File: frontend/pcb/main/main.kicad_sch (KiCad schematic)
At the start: 57 parts, among them J1 Ext, J10 Display1443, J2 CONN_01X02, J3 Display4020, J4 Debug, J5 RS485, J6 Conn_01x04, J7 Conn_01x02, J8 Conn_01x02, J9 Conn_01x02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

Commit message: Place remaining components.
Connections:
- net +12V: now also K1.4; no longer K1.3
- net GND: now also J2.2 (Pin_2); no longer J2.1 (Pin_1)
- new net: J2.1 (Pin_1), K1.3
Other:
- moved on the sheet: J2
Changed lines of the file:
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@@
     (stroke (width 0) (type solid))
+  )
+  (wire (pts (xy 231.14 143.51) (xy 231.14 138.43))
+    (stroke (width 0) (type default))
   )
   (wire (pts (xy 241.3 139.7) (xy 241.3 140.97))
@@
     (stroke (width 0) (type default))
   )
+  (wire (pts (xy 228.6 123.19) (xy 228.6 121.285))
+    (stroke (width 0) (type default))
+  )
   (wire (pts (xy 278.13 118.11) (xy 278.13 120.65))
     (stroke (width 0) (type default))
@@
     (stroke (width 0) (type default))
   )
+  (wire (pts (xy 219.71 149.86) (xy 217.17 149.86))
+    (stroke (width 0) (type default))
+  )
   (wire (pts (xy 124.46 44.45) (xy 147.955 44.45))
     (stroke (width 0) (type default))
@@
     (stroke (width 0) (type default))
   )
+  (wire (pts (xy 228.6 121.285) (xy 219.71 121.285))
+    (stroke (width 0) (type default))
+  )
   (wire (pts (xy 232.41 204.47) (xy 232.41 207.01))
     (stroke (width 0) (type default))
@@
   (wire (pts (xy 232.41 210.82) (xy 261.62 210.82))
     (stroke (width 0) (type default))
-  )
-  (wire (pts (xy 231.14 138.43) (xy 231.14 149.86))
-    (stroke (width 0) (type solid))
   )
   (wire (pts (xy 265.43 71.12) (xy 265.43 72.39))
@@
     (stroke (width 0) (type default))
   )
+  (wire (pts (xy 219.71 121.285) (xy 219.71 149.86))
+    (stroke (width 0) (type default))
+  )
   (wire (pts (xy 46.99 147.32) (xy 63.5 147.32))
     (stroke (width 0) (type default))
   )
-  (wire (pts (xy 228.6 113.03) (xy 228.6 123.19))
-    (stroke (width 0) (type solid))
-  )
   (wire (pts (xy 245.11 53.34) (xy 245.11 55.88))
     (stroke (width 0) (type default))
@@
   )
   (wire (pts (xy 200.66 216.535) (xy 200.66 217.805))
-    (stroke (width 0) (type default))
-  )
-  (wire (pts (xy 231.14 149.86) (xy 217.17 149.86))
     (stroke (width 0) (type default))
   )
@@
     (stroke (width 0) (type default))
   )
+  (wire (pts (xy 226.06 143.51) (xy 231.14 143.51))
+    (stroke (width 0) (type default))
+  )
   (wire (pts (xy 142.24 130.175) (xy 146.05 130.175))
     (stroke (width 0) (type default))
@@
   )
   (wire (pts (xy 132.08 147.955) (xy 132.08 159.385))
+    (stroke (width 0) (type default))
+  )
+  (wire (pts (xy 226.06 140.97) (xy 226.06 143.51))
     (stroke (width 0) (type default))
   )
@@
     )
   )
-  (symbol (lib_id "power:+12V") (at 228.6 113.03 0) (unit 1)
-    (exclude_from_sim no) (in_bom yes) (on_board yes) (dnp no) (fields_autoplaced)
-    (property "Reference" "#PWR04" (at 228.6 116.84 0)
-      (effects (font (size 1.27 1.27)) hide)
-    )
-    (property "Value" "+12V" (at 228.6 109.22 0)
+  (symbol (lib_id "power:+12V") (at 226.06 140.97 0) (unit 1)
+    (exclude_from_sim no) (in_bom yes) (on_board yes) (dnp no) (fields_autoplaced)
+    (property "Reference" "#PWR04" (at 226.06 144.78 0)
+      (effects (font (size 1.27 1.27)) hide)
+    )
+    (property "Value" "+12V" (at 226.06 137.16 0)
       (effects (font (size 1.27 1.27)))
     )
-    (property "Footprint" "" (at 228.6 113.03 0)
-      (effects (font (size 1.27 1.27)) hide)
-    )
-    (property "Datasheet" "" (at 228.6 113.03 0)
-      (effects (font (size 1.27 1.27)) hide)
-    )
-    (property "Description" "" (at 228.6 113.03 0)
+    (property "Footprint" "" (at 226.06 140.97 0)
+      (effects (font (size 1.27 1.27)) hide)
+    )
+    (property "Datasheet" "" (at 226.06 140.97 0)
+      (effects (font (size 1.27 1.27)) hide)
+    )
+    (property "Description" "" (at 226.06 140.97 0)
       (effects (font (size 1.27 1.27)) hide)
     )
@@
     )
   )
-  (symbol (lib_id "Connector_Generic:Conn_01x02") (at 212.09 152.4 180) (unit 1)
+  (symbol (lib_id "Connector_Generic:Conn_01x02") (at 212.09 149.86 0) (mirror y) (unit 1)
     (exclude_from_sim no) (in_bom yes) (on_board yes) (dnp no)
-    (property "Reference" "J2" (at 212.09 156.21 0)
+    (property "Reference" "J2" (at 212.09 146.05 0)
       (effects (font (size 1.27 1.27)))
     )
-    (property "Value" "CONN_01X02" (at 209.55 152.4 90)
-      (effects (font (size 1.27 1.27)) hide)
-    )
-    (property "Footprint" "Connector_JST:JST_XH_B2B-XH-A_1x02_P2.50mm_Vertical" (at 212.09 152.4 0)
-      (effects (font (size 1.27 1.27)) hide)
-    )
-    (property "Datasheet" "~" (at 212.09 152.4 0)
-      (effects (font (size 1.27 1.27)) hide)
-    )
-    (property "Description" "" (at 212.09 152.4 0)
-      (effects (font (size 1.27 1.27)) hide)
-    )
+    (property "Value" "CONN_01X02" (at 209.55 149.86 90)
+      (effects (font (size 1.27 1.27)) hide)
+    )
+    (property "Footprint" "Connector_JST:JST_XH_B2B-XH-A_1x02_P2.50mm_Vertical" (at 212.09 149.86 0)
+      (effects (font (size 1.27 1.27)) hide)
+    )
+    (property "Datasheet" "~" (at 212.09 149.86 0)
+      (effects (font (size 1.27 1.27)) hide)
+    )
+    (property "Description" "" (at 212.09 149.86 0)
+      (effects (font (size 1.27 1.27)) hide)
+    )

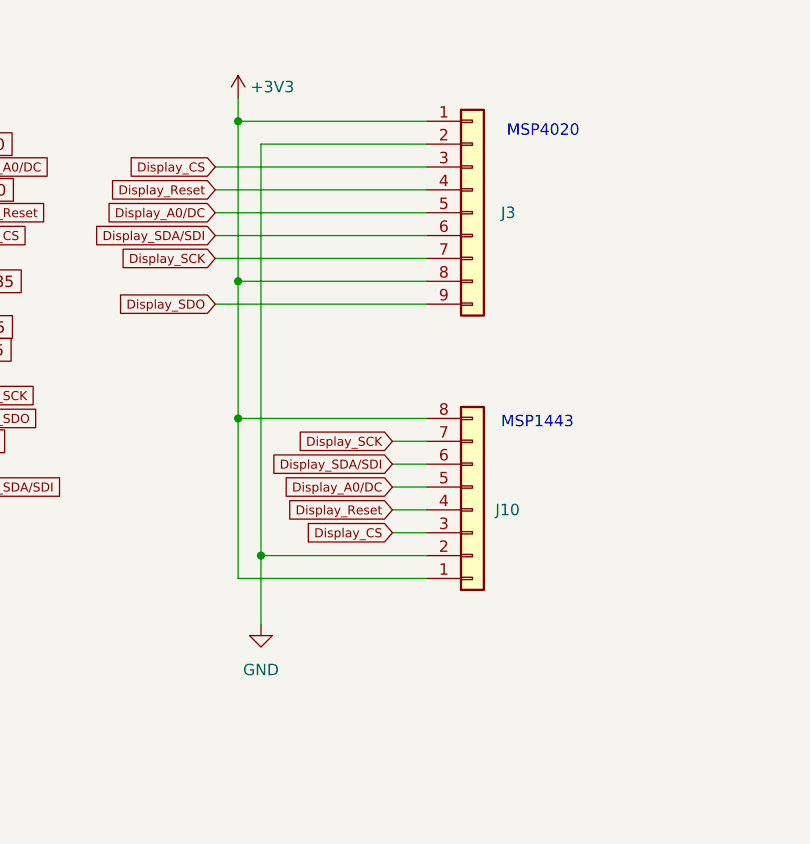
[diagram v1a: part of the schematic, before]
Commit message: Complete routing.
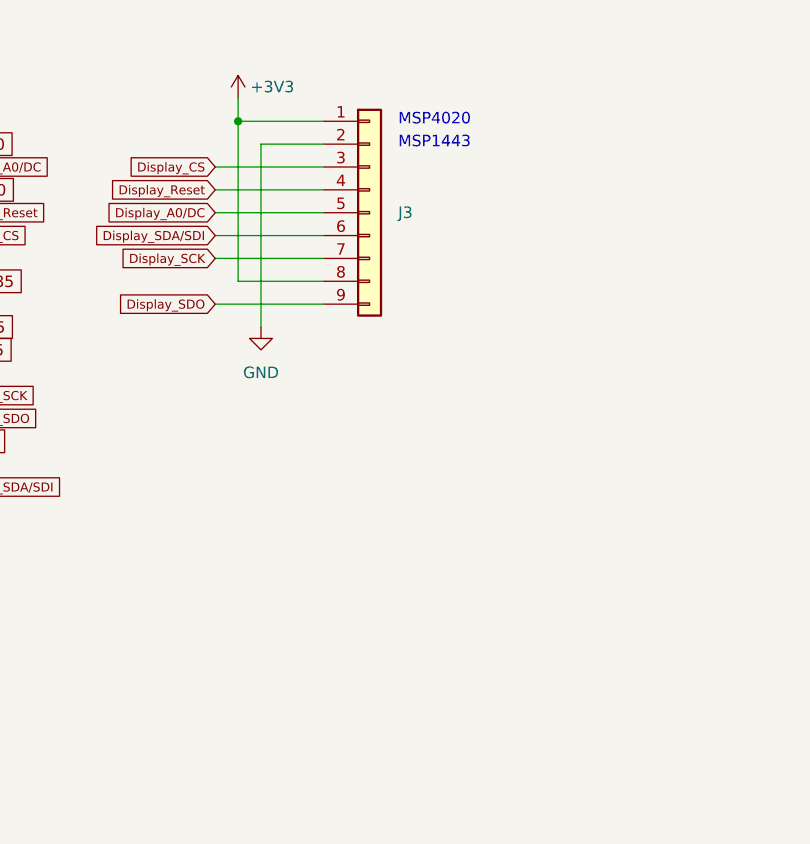
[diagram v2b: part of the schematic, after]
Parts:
- removed J10: Display1443, Connector_PinHeader_2.54mm:PinHeader_1x08_P2.54mm_Vertical, symbol Connector_Generic:Conn_01x08
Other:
- moved on the sheet: J3

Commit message: Update
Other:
- note added: "1-8: MSP1443"
- note added: "1-9: MSP3217, MSP4020"
- note removed: "MSP1443"
- note removed: "MSP4020"
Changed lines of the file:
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@@
     (effects (font (size 1.27 1.27)))
   )
-  (text "MSP1443" (exclude_from_sim no)
- (at 144.78 32.385 0)
+  (text "1-8: MSP1443" (exclude_from_sim no)
+ (at 144.78 33.02 0)
     (effects (font (size 1.27 1.27)) (justify left bottom))
   )
@@
     (effects (font (size 1.27 1.27)) (justify left bottom))
   )
-  (text "MSP4020" (exclude_from_sim no)
- (at 144.78 29.845 0)
+  (text "1-9: MSP3217, MSP4020" (exclude_from_sim no)
+ (at 144.78 30.48 0)
     (effects (font (size 1.27 1.27)) (justify left bottom))
   )
@@
   )
   (symbol (lib_id "Connector_Generic:Conn_01x09") (at 141.605 39.37 0) (unit 1)
-    (exclude_from_sim no) (in_bom yes) (on_board yes) (dnp no) (fields_autoplaced)
-    (property "Reference" "J3" (at 144.78 39.3699 0)
-      (effects (font (size 1.27 1.27)) (justify left))
-    )
+    (exclude_from_sim no) (in_bom yes) (on_board yes) (dnp no)
+    (property "Reference" "J3" (at 140.335 24.13 0)
+      (effects (font (size 1.27 1.27)) (justify left))
+    )
